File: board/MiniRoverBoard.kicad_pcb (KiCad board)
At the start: 2 copper layers, 38 parts, among them U2 OKI

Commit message: Add Layout
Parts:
- removed C7: 150nF, Capacitor_SMD:C_0603_1608Metric_Pad1.08x0.95mm_HandSolder
- removed C8: 4.7uF, Capacitor_SMD:C_0603_1608Metric_Pad1.08x0.95mm_HandSolder
- removed C9: 47uF, Capacitor_SMD:C_0603_1608Metric_Pad1.08x0.95mm_HandSolder
- removed D5: D, Diode_SMD:D_0603_1608Metric
- removed Molex4_5: DEBUG, MRDT_Connectors:MOLEX_SL_04_Vertical
- removed R18: 5k, Resistor_SMD:R_0603_1608Metric_Pad0.98x0.95mm_HandSolder
- removed R19: 1k, Resistor_SMD:R_0603_1608Metric_Pad0.98x0.95mm_HandSolder
- removed R20: 100, Resistor_SMD:R_0603_1608Metric_Pad0.98x0.95mm_HandSolder
- added B1: Buzzer, MRDT_Devices:BUZZER_SMI_1324_TW_5V_2_R, F.Cu at (147.2, 124.5)
- added C3: 10uF, Capacitor_SMD:C_0603_1608Metric_Pad1.08x0.95mm_HandSolder, F.Cu at (150.1, 75.2)
- added Conn6: Molex_SL_07, MRDT_Connectors:MOLEX_SL_07_Horizontal, F.Cu at (147.7, 115.5)
- added J1: DEBUG, Connector_PinSocket_2.54mm:PinSocket_1x04_P2.54mm_Vertical, F.Cu at (118.4, 119.7)
- added Q1: NMOS, Package_TO_SOT_THT:TO-220-3_Vertical, F.Cu at (151.2, 71.9)
- added Q2: BSS138, Package_TO_SOT_SMD:SOT-23, F.Cu at (163.2, 76.3)
- added R3: 5.1k, Resistor_SMD:R_0603_1608Metric_Pad0.98x0.95mm_HandSolder, F.Cu at (150.1, 77.7)
- added U3: Opamp_Dual, Package_SO:SO-8_3.9x4.9mm_P1.27mm, F.Cu at (160.0, 53.3)
- added U4: LT1910, Package_SO:SOIC-8_3.9x4.9mm_P1.27mm, F.Cu at (156.5, 77.3)
- added U7: ESP32-S2-DEVKITM-1U, MRDT_Shields:XCVR_ESP32-S2-DEVKITM-1U, F.Cu at (102.6, 95.8)
- added U8: Opamp_Dual, Package_SO:SO-8_3.9x4.9mm_P1.27mm, F.Cu at (241.3, 73.7)
- C5: footprint Capacitor_SMD:C_0603_1608Metric_Pad1.08x0.95mm_HandSolder -> Capacitor_THT:CP_Radial_D10.0mm_P5.00mm
- Conn2, Conn3: footprint MRDT_Connectors:Anderson_2_Horizontal_Side_by_Side -> MRDT_Connectors:Square_Anderson_2_H_Side_By_Side_PV
- Conn4, Molex4_4, Molex4_6, Molex4_7: footprint MRDT_Connectors:MOLEX_SL_04_Vertical -> MRDT_Connectors:MOLEX_SL_04_Horizontal
- Conn5: footprint MRDT_Connectors:MOLEX_SL_04_Vertical -> MRDT_Connectors:MOLEX_SL_09_Horizontal
- Molex4_1: value OLED display -> I2C_BUS; footprint MRDT_Connectors:MOLEX_SL_04_Vertical -> MRDT_Connectors:MOLEX_SL_04_Horizontal
- R16: value R_US -> 4.7K
- R17: value 5k -> 4.7K
- U2: footprint Converter_DCDC:Converter_DCDC_Murata_OKI-78SR_Horizontal -> MRDT_Devices:OKI_Horizontal
- moved Conn4 128.2 mm to (237.5, 54.4)
- moved R14 119.9 mm to (236.2, 63.5)
- moved R15 111.9 mm to (228.6, 68.6)
- moved C5 76.3 mm to (124.2, 123.2)
- moved D1 73.8 mm to (182.8, 91.3)
- moved D2 73.8 mm to (182.8, 93.9)
- moved U2 73.8 mm to (172.1, 82.1)
- moved C1 73.8 mm to (182.8, 81.3)
- moved C2 73.8 mm to (182.8, 83.8)
- moved R1 73.8 mm to (182.8, 86.3)
- moved R2 73.8 mm to (182.8, 88.8)
- moved R6 71.8 mm to (152.4, 48.3)
- moved Conn5 65.5 mm to (119.8, 115.5)
- moved R5 64.9 mm to (170.8, 71.7)
- moved R9 64.9 mm to (175.2, 71.7)
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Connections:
- Conn5 pad 1: GPIO 10 -> ESC_PWM_6
- Conn5 pad 2: GPIO 9 -> ESC_PWM_5
- Conn5 pad 3: GPIO 8 -> ESC_PWM_4
- Conn5 pad 4: GPIO 7 -> ESC_PWM_3
- Molex4_1 pad 1: GND -> +5V
- Molex4_1 pad 2: +5V -> SDA
- Molex4_1 pad 3: GPIO 45 -> SCL
- Molex4_1 pad 4: GPIO 44 -> GND
- R16 pad 1: Net-(U1-ILIMIT) -> +5V
- R16 pad 2: GND -> SCL
- R17 pad 1: Net-(U1-IN) -> SDA
- R17 pad 2: Net-(D5-A) -> +5V

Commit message: started layout with all footprints
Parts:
- moved Molex4_1 184.2 mm to (269.5, 18.1), turned to -90 degrees
- moved Molex4_4 166.0 mm to (269.5, 33.2), turned to -90 degrees
- moved Molex4_6 148.7 mm to (269.5, 48.3), turned to -90 degrees
- moved Q1 135.4 mm to (275.5, 125.5), turned to -90 degrees
- moved Molex4_7 132.5 mm to (269.5, 63.4), turned to -90 degrees
- moved R17 128.4 mm to (261.5, 18.9), turned to 90 degrees
- moved C3 126.4 mm to (264.0, 130.0), turned to 90 degrees
- moved R16 124.9 mm to (259.0, 18.9), turned to 90 degrees
- moved C5 121.9 mm to (52.0, 25.0), turned to 90 degrees
- moved Conn2 116.0 mm to (42.0, 18.8)
- moved Conn3 115.5 mm to (41.5, 37.8)
- moved U4 106.4 mm to (254.5, 118.6)
- moved Conn5 96.1 mm to (24.4, 104.0), turned to 90 degrees
- moved U3 86.6 mm to (76.0, 32.5), turned to 90 degrees
- moved Conn4 39.9 mm to (269.5, 78.2), turned to -90 degrees
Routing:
- net GND: track 0.00 -> 159.8 mm
- net +12V: track 0.00 -> 11.0 mm
- net ESC_PWR: track 0.00 -> 3.37 mm

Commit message: got footprints laid out
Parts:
- moved Molex4_1 258.1 mm to (26.5, 104.9), turned to 90 degrees
- moved Molex4_4 250.1 mm to (26.1, 90.8), turned to 90 degrees
- moved Molex4_6 244.9 mm to (26.1, 75.7), turned to 90 degrees
- moved Q1 244.7 mm to (48.5, 34.0)
- moved Molex4_7 243.4 mm to (26.1, 61.2), turned to 90 degrees
- moved U4 214.9 mm to (62.5, 22.1), turned to 180 degrees
- moved C3 214.2 mm to (75.0, 29.1), turned to -90 degrees
- moved R17 207.4 mm to (59.5, 66.0)
- moved Conn4 206.1 mm to (65.0, 53.0)
- moved R16 200.2 mm to (64.0, 64.5), turned to -90 degrees
- moved U8 177.4 mm to (71.6, 22.1)
- moved R14 172.1 mm to (67.6, 29.0), turned to 90 degrees
- moved R15 165.3 mm to (68.9, 26.0)
- moved C2 157.3 mm to (27.5, 109.0)
- moved R5 135.0 mm to (37.1, 53.5)
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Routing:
- net GND: track 159.8 -> 4.80 mm
- net +12V: track 11.0 -> 0.00 mm
- net ESC_PWR: track 3.37 -> 2.52 mm

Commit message: added pmos channel (still need footprints not working)
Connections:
- C5 pad 2: GND -> Net-(MOSFET2-GATE)
- Conn2 pad 4: +12V -> (no net)
- Conn3 pad 4: ESC_PWR -> (no net)
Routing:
- net Net-(MOSFET2-GATE): track 0.00 -> 1.33 mm
- net GND: track 4.80 -> 3.48 mm
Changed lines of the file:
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@@
 	(net 60 "unconnected-(U8-Pad7)")
 	(net 61 "unconnected-(U8B-+-Pad5)")
+	(net 62 "Net-(MOSFET2-GATE)")
 	(footprint "MRDT_Connectors:MOLEX_SL_04_Horizontal"
 		(layer "F.Cu")
@@
 			(layers "*.Cu" "*.Mask")
 			(remove_unused_layers no)
-			(net 2 "+12V")
 		)
 		(embedded_fonts no)
@@
 			(layers "*.Cu" "*.Mask")
 			(remove_unused_layers no)
-			(net 1 "GND")
+			(net 62 "Net-(MOSFET2-GATE)")
 			(pintype "passive")
 		)
@@
 			(layers "*.Cu" "*.Mask")
 			(remove_unused_layers no)
-			(net 7 "ESC_PWR")
 		)
 		(embedded_fonts no)
@@
 	)
 	(segment
-		(start 51.063 19.063)
-		(end 52 20)
-		(width 0.2)
-		(layer "F.Cu")
-		(net 1)
-	)
-	(segment
 		(start 71.5 29.8625)
 		(end 71.6525 29.8625)
@@
 		(net 26)
 	)
+	(segment
+		(start 51.063 19.063)
+		(end 52 20)
+		(width 0.2)
+		(layer "F.Cu")
+		(net 62)
+	)
 	(embedded_fonts no)

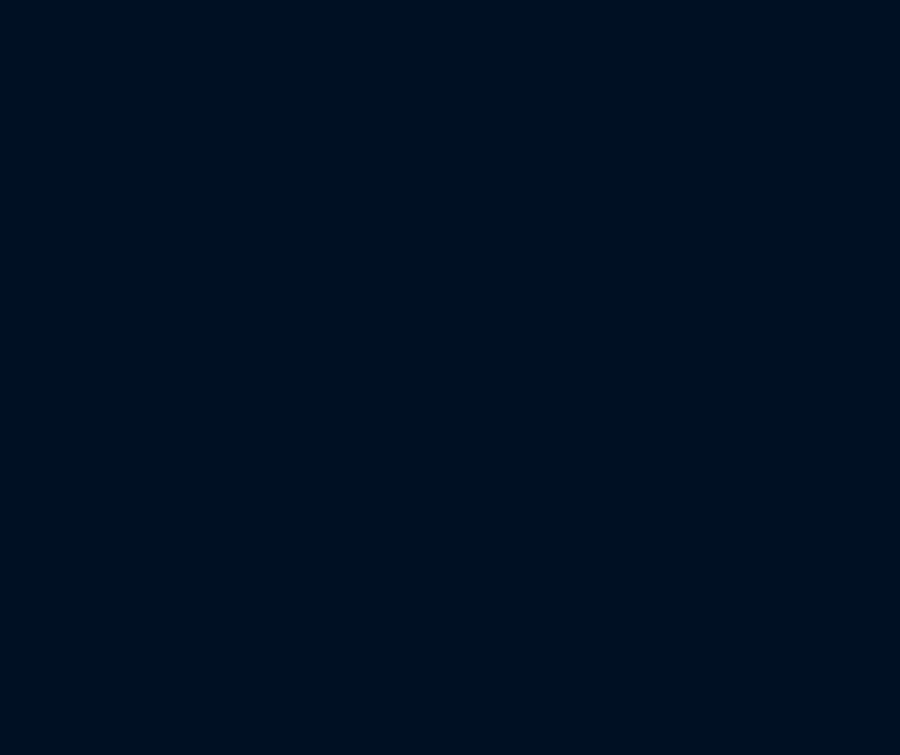
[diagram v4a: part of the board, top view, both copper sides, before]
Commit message: Add resistor footprints for p-channel mosfets
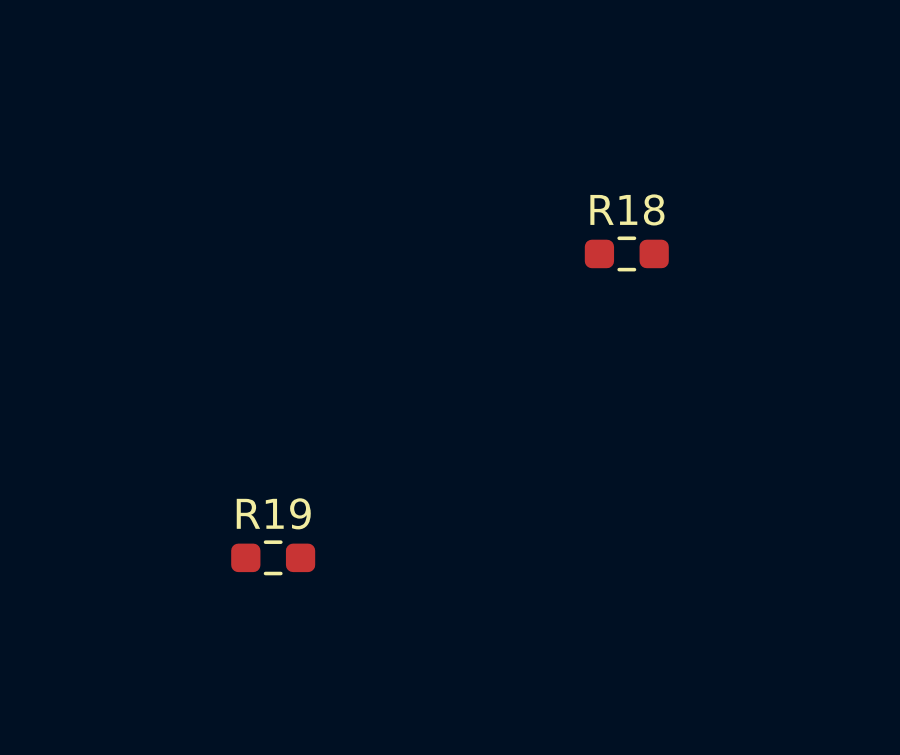
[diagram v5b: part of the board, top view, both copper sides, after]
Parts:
- added R18: 10k, Resistor_SMD:R_0603_1608Metric_Pad0.98x0.95mm_HandSolder, F.Cu at (141.3, 66.1)
- added R19: 10k, Resistor_SMD:R_0603_1608Metric_Pad0.98x0.95mm_HandSolder, F.Cu at (129.5, 76.2)

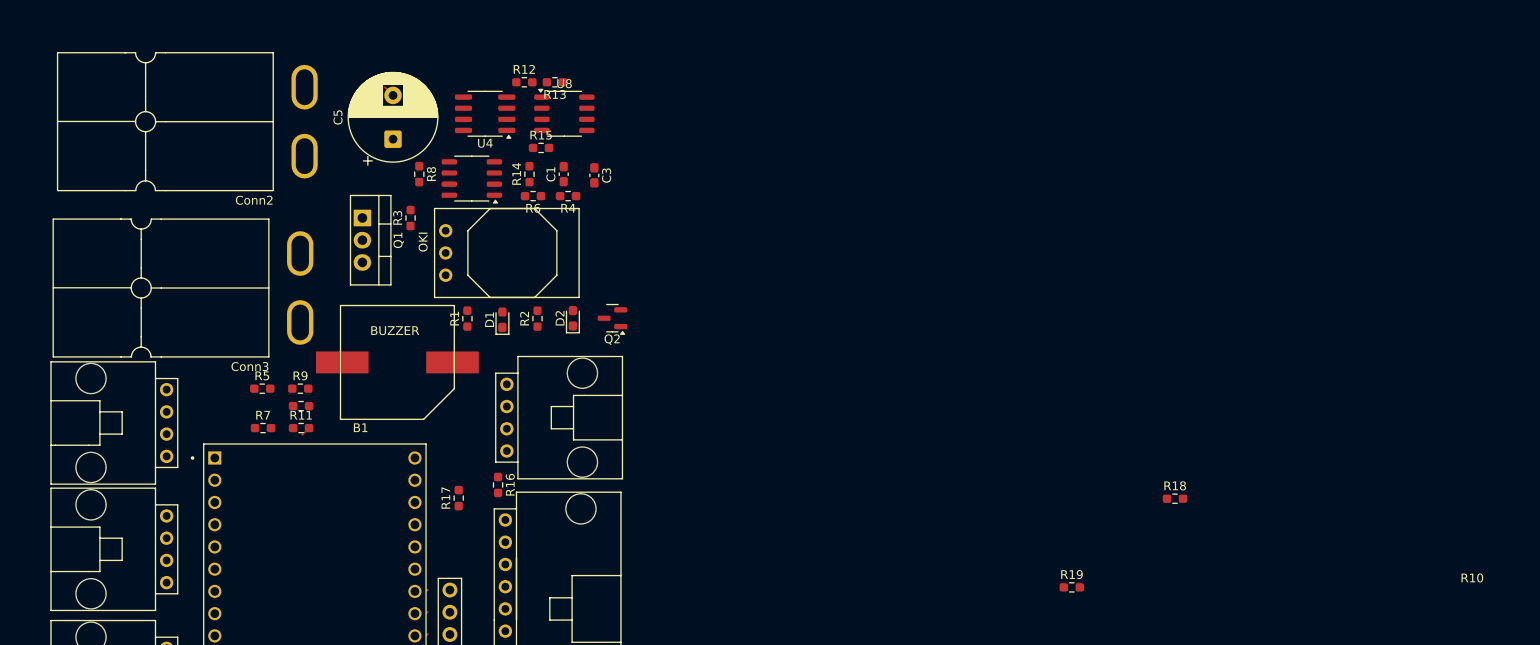
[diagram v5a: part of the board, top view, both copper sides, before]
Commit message: Add p-channel MOSFETs to Layout
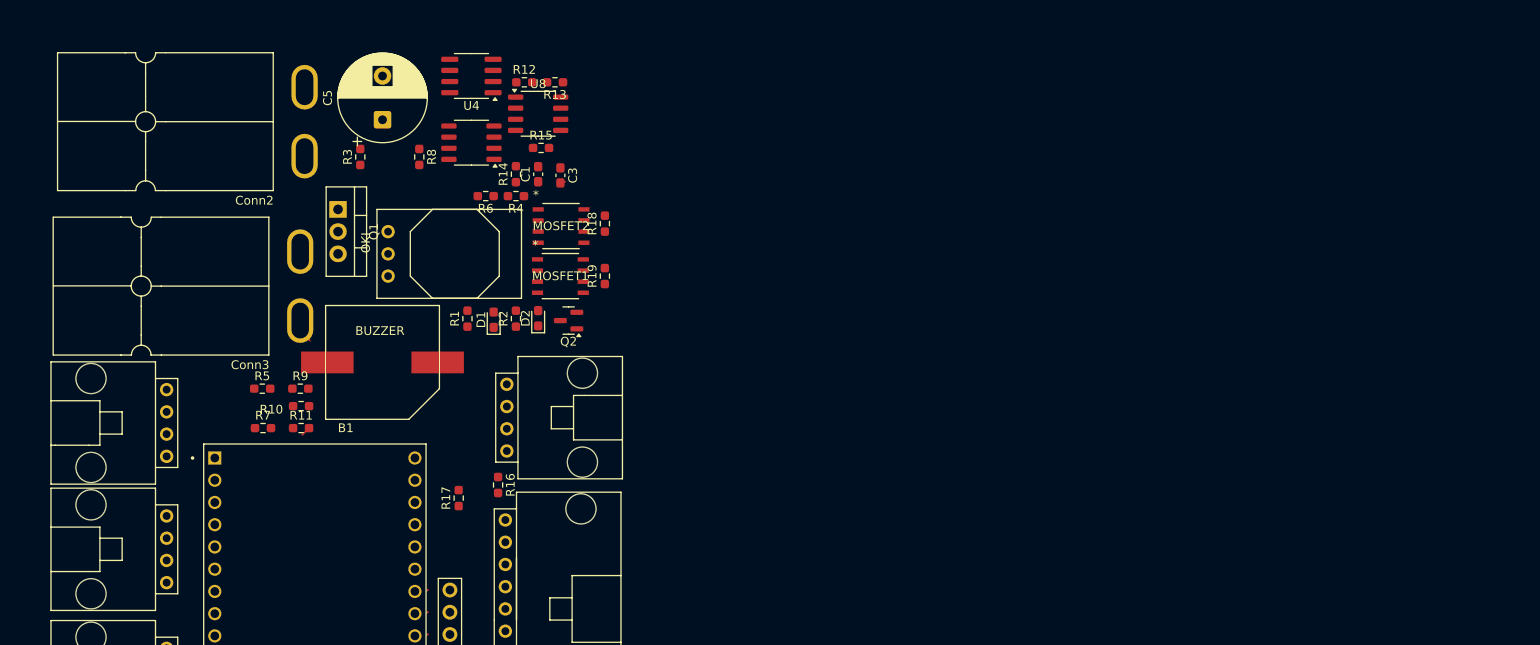
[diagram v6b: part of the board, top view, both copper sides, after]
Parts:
- added MOSFET1: TPC8132_LQS, MRDT_Devices:SOP-8_TOS-L, F.Cu at (71.1, 40.6)
- added MOSFET2: TPC8132_LQS, MRDT_Devices:SOP-8_TOS-L, F.Cu at (71.2, 34.9)
- moved R18 72.3 mm to (76.2, 34.6), turned to 90 degrees
- moved R19 64.1 mm to (76.2, 40.6), turned to 90 degrees
- moved R3 9.03 mm to (48.3, 27.0)
- moved U2 6.58 mm to (51.4, 40.6)
- moved R4 5.96 mm to (66.0, 31.5)
- moved R6 5.41 mm to (62.6, 31.5)
- moved Q2 5.01 mm to (72.1, 45.7)
- moved U4 4.59 mm to (61.0, 17.8)
- moved U3 4.10 mm to (61.0, 25.4)
- moved D2 3.97 mm to (68.6, 45.5)
- moved C3 3.88 mm to (71.1, 29.1)
- moved U8 3.00 mm to (68.6, 22.1)
- moved Q1 2.95 mm to (45.7, 33.0)
- moved C1 2.92 mm to (68.6, 29.0)
- moved C5 2.52 mm to (50.8, 22.8)
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
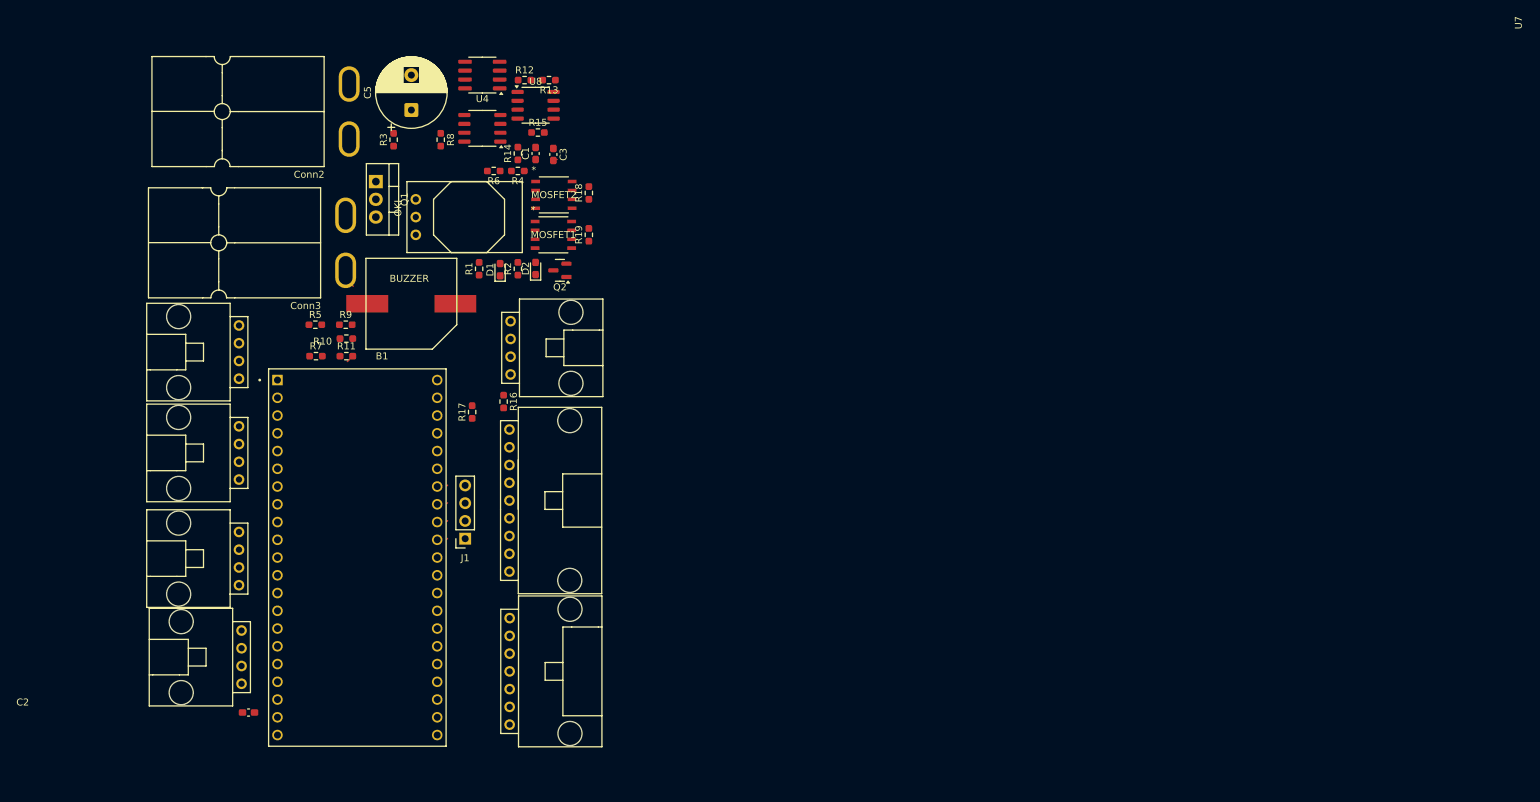
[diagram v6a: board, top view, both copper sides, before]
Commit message: Layout started with initial dimensions
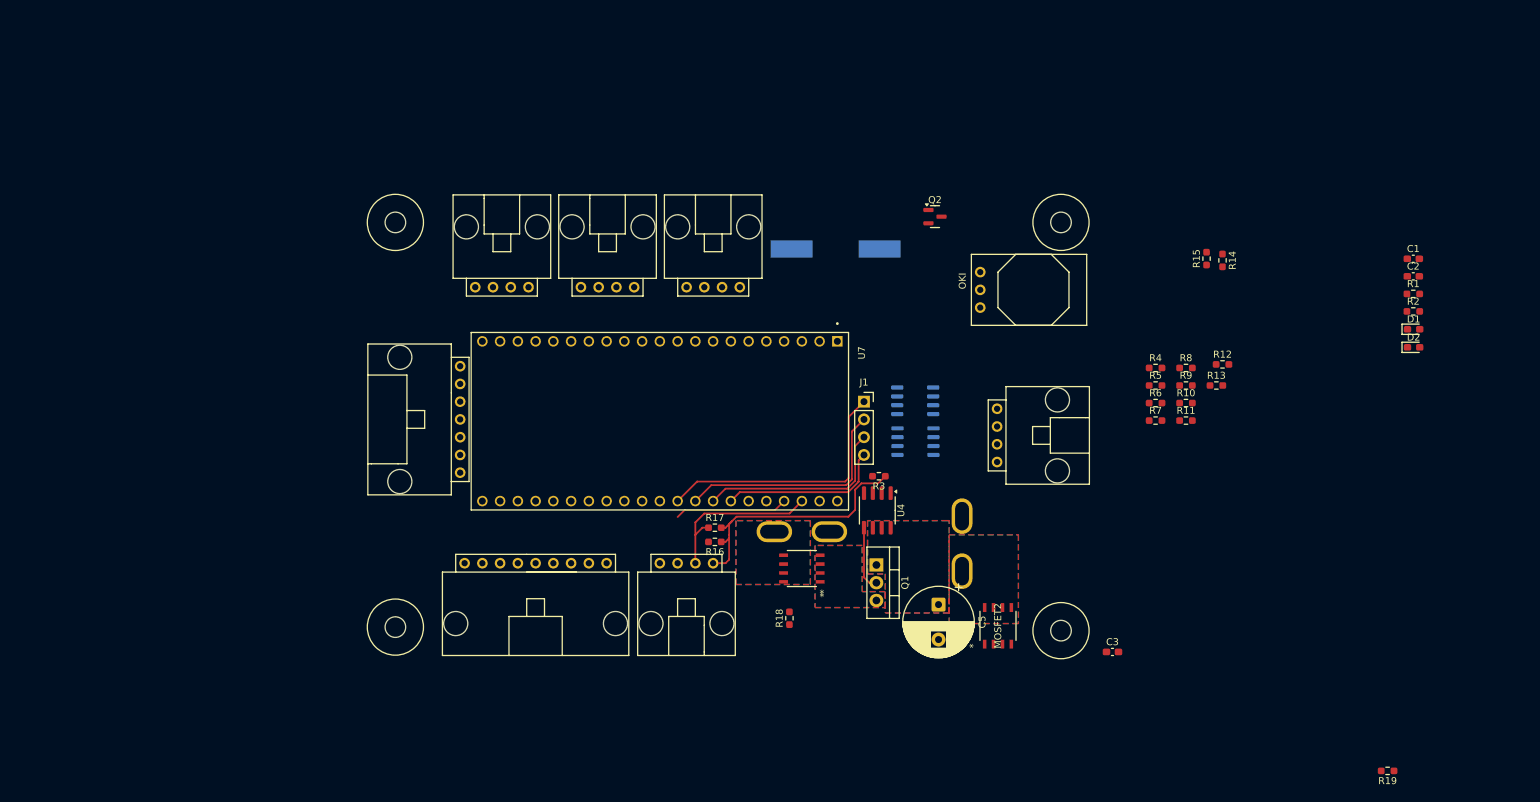
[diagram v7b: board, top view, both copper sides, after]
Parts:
- added H1: MountingHole, MRDT_Drill_Holes:4_40_Hole, F.Cu at (143.8, 97.3)
- added H2: MountingHole, MRDT_Drill_Holes:4_40_Hole, F.Cu at (48.5, 96.8)
- added H3: MountingHole, MRDT_Drill_Holes:4_40_Hole, F.Cu at (143.8, 38.9)
- added H4: MountingHole, MRDT_Drill_Holes:4_40_Hole, F.Cu at (48.5, 38.9)
- B1, Conn2, Conn3, U3, U8: moved to B.Cu
- moved C2 178.0 mm to (194.2, 46.6)
- moved R19 137.7 mm to (190.5, 117.3), turned to 180 degrees
- moved R1 133.7 mm to (194.2, 49.1), turned to 0 degrees
- moved D1 131.0 mm to (194.2, 54.1), turned to 0 degrees
- moved R2 128.3 mm to (194.2, 51.6), turned to 0 degrees
- moved C1 126.5 mm to (194.2, 44.1), turned to 0 degrees
- moved D2 126.1 mm to (194.2, 56.7), turned to 0 degrees
- moved R5 120.5 mm to (157.3, 62.2)
- moved R9 120.5 mm to (161.6, 62.2)
- moved R10 120.5 mm to (161.6, 64.7), turned to 0 degrees
- moved R11 120.5 mm to (161.6, 67.2)
- moved R7 120.5 mm to (157.3, 67.2)
- moved R8 111.5 mm to (161.6, 59.7), turned to 0 degrees
- moved R12 107.8 mm to (166.9, 59.2)
- moved Conn2 107.1 mm to (129.5, 80.6), turned to 180 degrees
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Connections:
- Conn2 pad 4: (no net) -> Net-(Conn2B-V+Log)
- Conn3 pad 4: (no net) -> Net-(Conn3B-V+Log)
- MOSFET1 pad 1: unconnected-(MOSFET1-SOURCE-Pad1) -> ESC_PWR
- MOSFET1 pad 2: unconnected-(MOSFET1-SOURCE-Pad2) -> ESC_PWR
- MOSFET1 pad 5: unconnected-(MOSFET1-DRAIN-Pad5) -> Net-(Conn3B-V+Log)
- MOSFET1 pad 6: unconnected-(MOSFET1-DRAIN-Pad6) -> Net-(Conn3B-V+Log)
- MOSFET1 pad 7: unconnected-(MOSFET1-DRAIN-Pad7) -> Net-(Conn3B-V+Log)
- MOSFET2 pad 1: unconnected-(MOSFET2-SOURCE-Pad1) -> +12V
- MOSFET2 pad 2: unconnected-(MOSFET2-SOURCE-Pad2) -> +12V
- MOSFET2 pad 5: unconnected-(MOSFET2-DRAIN-Pad5) -> Net-(Conn2B-V+Log)
- MOSFET2 pad 6: unconnected-(MOSFET2-DRAIN-Pad6) -> Net-(Conn2B-V+Log)
- MOSFET2 pad 7: unconnected-(MOSFET2-DRAIN-Pad7) -> Net-(Conn2B-V+Log)
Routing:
- net MTCK: track 0.17 -> 37.7 mm
- net +5V: track 0.47 -> 37.7 mm
- net MTDO: track 0.17 -> 33.0 mm
- net MTDI: track 0.17 -> 28.3 mm
- net SDA: track 0.00 -> 24.6 mm
- net MTMS: track 0.17 -> 23.6 mm
- net SCL: track 0.00 -> 16.2 mm
- net Net-(Q1-G): track 0.00 -> 9.21 mm
- net GND: track 3.48 -> 0.00 mm
- net ESC_PWR: track 2.52 -> 0.00 mm
- net Net-(MOSFET2-GATE): track 1.33 -> 0.00 mm
- added copper zone on B.Cu, net +12V
- added copper zone on F.Cu, net +12V
- added copper zone on B.Cu, net ESC_PWR
- added copper zone on F.Cu, net ESC_PWR
- added copper zone on B.Cu, net Net-(Conn2B-V+Log)
- added copper zone on F.Cu, net Net-(Conn2B-V+Log)
- added copper zone on B.Cu, net Net-(Conn3B-V+Log)
- added copper zone on F.Cu, net Net-(Conn3B-V+Log)
